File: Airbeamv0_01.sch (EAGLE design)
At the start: 91 parts

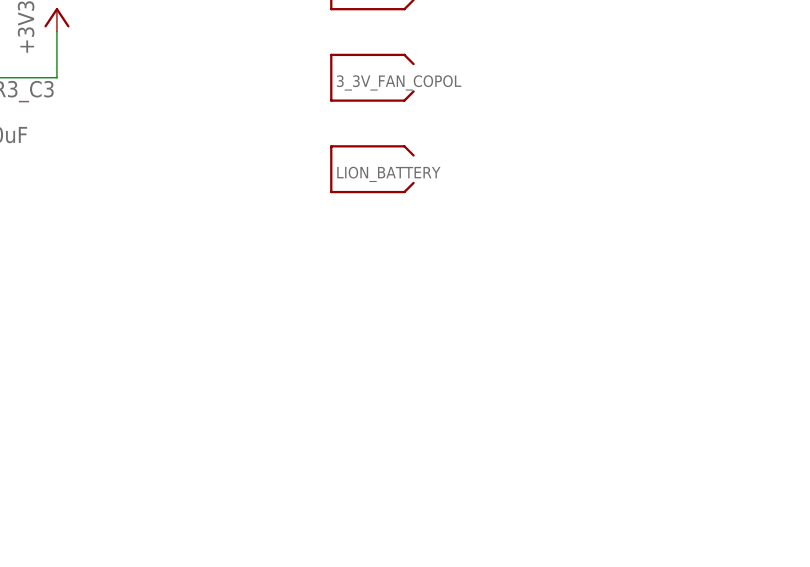
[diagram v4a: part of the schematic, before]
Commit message: changed bead to one in stock
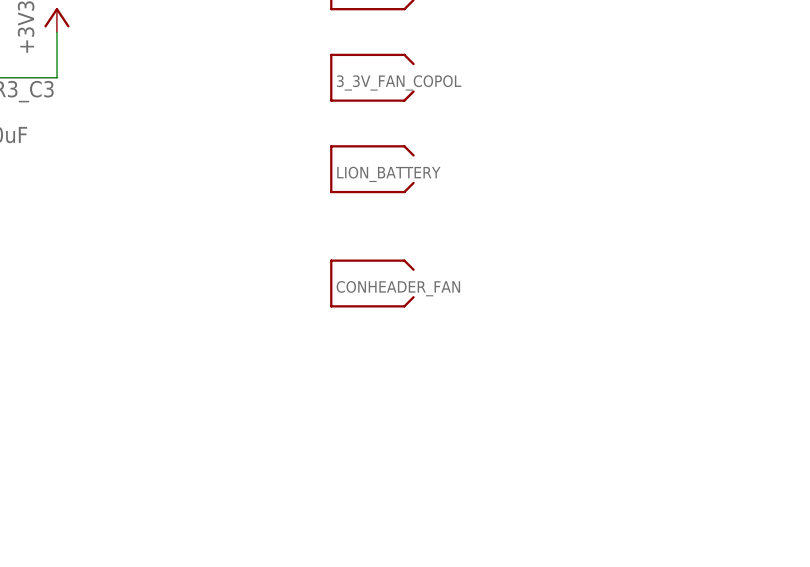
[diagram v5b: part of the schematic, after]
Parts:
- added CONHEADER_FAN: OFF_BOARD, Airbeam:PART_OFFBOARD
- CA_FB1, U_FB1, U_FB2: PARTNO MH2029-300Y -> MH2029-600Y
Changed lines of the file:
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@@
 <part name="GND47" library="supply1" deviceset="GND" device=""/>
 <part name="U_FB1" library="Airbeam" deviceset="FERITE_BEAD" device="">
-<attribute name="PARTNO" value="MH2029-300Y"/>
+<attribute name="PARTNO" value="MH2029-600Y"/>
 </part>
 <part name="CA_FB1" library="Airbeam" deviceset="FERITE_BEAD" device="">
-<attribute name="PARTNO" value="MH2029-300Y"/>
+<attribute name="PARTNO" value="MH2029-600Y"/>
 </part>
 <part name="U_FB2" library="Airbeam" deviceset="FERITE_BEAD" device="">
-<attribute name="PARTNO" value="MH2029-300Y"/>
+<attribute name="PARTNO" value="MH2029-600Y"/>
 </part>
 <part name="U$1" library="Airbeam" deviceset="MOSFET-N" device=""/>
@@
 </part>
 <part name="U$2" library="Airbeam" deviceset="SUR_2PIN" device=""/>
+<part name="CONHEADER_FAN" library="Airbeam" deviceset="PART_OFFBOARD" device="" value="OFF_BOARD">
+<attribute name="PARTNO" value="02SUR-32S"/>
+</part>
 </parts>
 <sheets>
@@
 </instance>
 <instance part="U$2" gate="G$1" x="-76.2" y="-167.64"/>
+<instance part="CONHEADER_FAN" gate="G$1" x="276.86" y="-38.1">
+<attribute name="PARTNO" x="276.86" y="-38.1" size="1.778" layer="96" display="off"/>
+</instance>
 </instances>
 <busses>

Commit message: updated parts, haven't updated BOM
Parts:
- VR5_L1: PARTNO NRS5020T6R8MMGJ -> RT6150BGQW
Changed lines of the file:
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@@
 <part name="GND22" library="supply1" deviceset="GND" device=""/>
 <part name="VR5_L1" library="SparkFun-Passives" deviceset="INDUCTOR" device="1210" value="6uH">
-<attribute name="PARTNO" value="NRS5020T6R8MMGJ"/>
+<attribute name="PARTNO" value="RT6150BGQW"/>
 </part>
 <part name="P+7" library="supply1" deviceset="+5V" device=""/>
